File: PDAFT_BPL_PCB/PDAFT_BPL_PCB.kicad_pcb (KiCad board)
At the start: 2 copper layers, 63.4 x 85.5 mm, 19 parts

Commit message: board update
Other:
- board text added: "LEDs"

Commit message: Update for DIY-make
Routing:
- added copper zone on B.Cu, net (none)

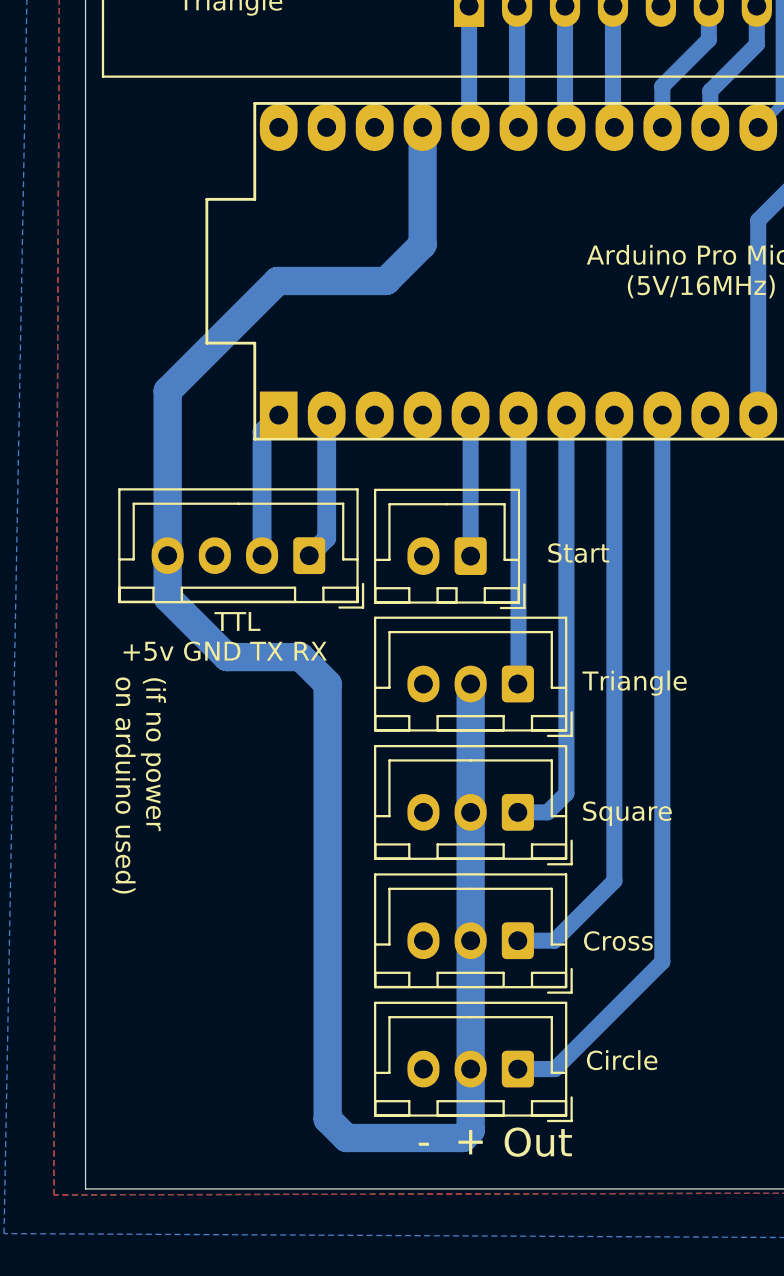
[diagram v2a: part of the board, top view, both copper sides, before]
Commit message: Added shorter variant, maybe later it will be main
Also some elements optimization
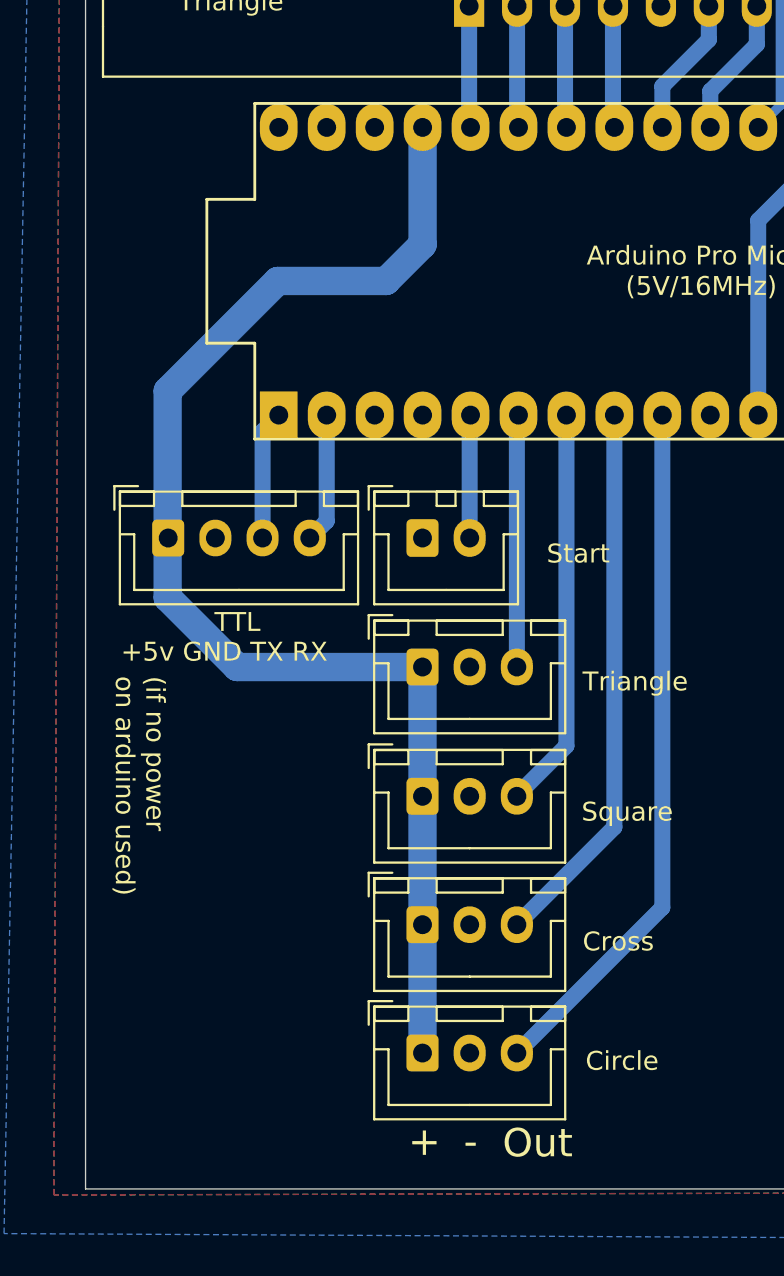
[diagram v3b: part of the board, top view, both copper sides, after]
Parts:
- moved TTL1 7.53 mm to (106.0, 81.5), turned to 0 degrees
- moved Triangle1 5.13 mm to (119.5, 88.3), turned to 0 degrees
- moved Circle1 5.12 mm to (119.5, 108.8), turned to 0 degrees
- moved Cross1 5.12 mm to (119.5, 102.0), turned to 0 degrees
- moved Square1 5.12 mm to (119.5, 95.2), turned to 0 degrees
- moved Start1 2.72 mm to (119.5, 81.5), turned to 0 degrees
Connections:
- Circle1 pad 1: Net-(Circle1-Pad1) -> Net-(ProMicro1-Pad21)
- Circle1 pad 2: Net-(Circle1-Pad2) -> Net-(12V_IN1-Pad3)
- Circle1 pad 3: Net-(12V_IN1-Pad3) -> Net-(ProMicro1-Pad9)
- Cross1 pad 1: Net-(Cross1-Pad1) -> Net-(ProMicro1-Pad21)
- Cross1 pad 2: Net-(Circle1-Pad2) -> Net-(12V_IN1-Pad3)
- Cross1 pad 3: Net-(12V_IN1-Pad3) -> Net-(ProMicro1-Pad8)
- ProMicro1 pad 1: Net-(ProMicro1-Pad1) -> Net-(TTL1-Pad3)
- ProMicro1 pad 2: Net-(ProMicro1-Pad2) -> Net-(TTL1-Pad4)
- ProMicro1 pad 21: Net-(Circle1-Pad2) -> Net-(ProMicro1-Pad21)
- ProMicro1 pad 8: Net-(Cross1-Pad1) -> Net-(ProMicro1-Pad8)
- ProMicro1 pad 9: Net-(Circle1-Pad1) -> Net-(ProMicro1-Pad9)
- Square1 pad 1: Net-(ProMicro1-Pad7) -> Net-(ProMicro1-Pad21)
- Square1 pad 2: Net-(Circle1-Pad2) -> Net-(12V_IN1-Pad3)
- Square1 pad 3: Net-(12V_IN1-Pad3) -> Net-(ProMicro1-Pad7)
- Start1 pad 1: Net-(ProMicro1-Pad5) -> Net-(12V_IN1-Pad3)
- Start1 pad 2: Net-(12V_IN1-Pad3) -> Net-(ProMicro1-Pad5)
- TTL1 pad 1: Net-(ProMicro1-Pad2) -> Net-(ProMicro1-Pad21)
- TTL1 pad 2: Net-(ProMicro1-Pad1) -> Net-(12V_IN1-Pad3)
- TTL1 pad 3: Net-(12V_IN1-Pad3) -> Net-(TTL1-Pad3)
- TTL1 pad 4: Net-(Circle1-Pad2) -> Net-(TTL1-Pad4)
- Triangle1 pad 1: Net-(ProMicro1-Pad6) -> Net-(ProMicro1-Pad21)
- Triangle1 pad 2: Net-(Circle1-Pad2) -> Net-(12V_IN1-Pad3)
- Triangle1 pad 3: Net-(12V_IN1-Pad3) -> Net-(ProMicro1-Pad6)
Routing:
- net Net-(Circle1-Pad2): track 99.0 -> 0.00 mm
- net Net-(ProMicro1-Pad21): track 0.00 -> 69.3 mm
- net Net-(Circle1-Pad1): track 39.4 -> 0.00 mm
- net Net-(ProMicro1-Pad9): track 0.00 -> 37.0 mm
- net Net-(Cross1-Pad1): track 31.4 -> 0.00 mm
- net Net-(ProMicro1-Pad8): track 0.00 -> 29.1 mm
- net Net-(ProMicro1-Pad2): track 7.83 -> 0.00 mm
- net Net-(ProMicro1-Pad1): track 7.81 -> 0.00 mm
- net Net-(TTL1-Pad4): track 0.00 -> 6.88 mm
- net Net-(TTL1-Pad3): track 0.00 -> 6.87 mm
- net Net-(ProMicro1-Pad7): track 23.1 -> 21.3 mm
- net Net-(ProMicro1-Pad6): track 14.6 -> 13.5 mm
- net Net-(ProMicro1-Pad5): track 7.76 -> 6.83 mm
